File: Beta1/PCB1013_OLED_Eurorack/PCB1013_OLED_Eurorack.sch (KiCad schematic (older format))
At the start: 41 parts, among them J1 Axoloti_40Pin, J2 FPC_20POS, U1 MCP3008T-I/SL, U10 OLED_128x32_I2C, U2 MCP3008T-I/SL, U20 OLED_128x32_I2C, U3 I2C_1x4MUX_TCA9546A, U30 OLED_128x32_I2C, U40 OLED_128x32_I2C

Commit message: Rough placement
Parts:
- removed C1, C2: 0.1u, Capacitors_SMD:C_0603, symbol C
- removed CS_0_7, GND0, SPI_CLK_0, SPI_MISO_0, SPI_MOSI_0, VCC0: CONN_01X01, Liberry:single_0.1, symbol CONN_01X01
- removed JOY0, JOY1, JOY2, JOY3: XYJOY_Alps, Liberry:JOY_ALPS_RKJXV1224005, symbol XYJOY_Alps
- removed R0, R1, R2, R3, R4, R5, R6, R7: POT, Liberry:POT_ALPS_RK09K1130BM4, symbol POT
- removed U1, U2: MCP3008T-I/SL, Liberry:SOIC-16, symbol MCP3008T-I/SL
- added C4: 0.1u, Capacitor_SMD:C_0603_1608Metric, symbol Device:C
- added R4, RC1, RC50, RC60, RC70, RC80, RD1, RD50, RD60, RD70, RD80, RR1: 10K, Resistor_SMD:R_0603_1608Metric, symbol Device:R
- added U4: I2C_1x4MUX_TCA9546A, Liberry:SOIC-16_1.27x5.4, symbol PCB1013_OLED_Eurorack-rescue:I2C_1x4MUX_TCA9546A
- added U50, U60, U70, U80: OLED_128x32_I2C, Liberry:OLED_128x32, symbol PCB1013_OLED_Eurorack-rescue:OLED_128x32_I2C
- added U5000: STM32F103C8T6_BLUE_PILL, Liberry:BLUEPILL_CORTEXM3_STM32F103C8T6_THIN, symbol PCB1013_OLED_Eurorack:STM32F103C8T6_BLUE_PILL
- C3: symbol C -> Device:C
- J1: symbol Axoloti_40Pin -> PCB1013_OLED_Eurorack-rescue:Axoloti_40Pin
- J2: symbol FPC_20POS -> PCB1013_OLED_Eurorack-rescue:FPC_20POS
- RC0, RC10, RC20, RC30, RC40, RD0, RD10, RD20, RD30, RD40, RR0: footprint Resistors_SMD:R_0603 -> Resistor_SMD:R_0603_1608Metric; symbol R -> Device:R
- U10, U20, U30, U40: symbol OLED_128x32_I2C -> PCB1013_OLED_Eurorack-rescue:OLED_128x32_I2C
- U3: symbol I2C_1x4MUX_TCA9546A -> PCB1013_OLED_Eurorack-rescue:I2C_1x4MUX_TCA9546A
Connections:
- net labels added: I2C_SCL4, I2C_SCL5, I2C_SCL6, I2C_SCL7, I2C_SCL_AXO, I2C_SCL_EXT, I2C_SC_AXO, I2C_SDA4, I2C_SDA5, I2C_SDA6, I2C_SDA7, I2C_SDA_AXO, I2C_SDA_EXT, RESET_AXO, RX_AXO, RX_EXT, TX_AXO, TX_EXT
- net labels removed: I2C_SCL, I2C_SDA, JOY_0_0, JOY_0_1, JOY_1_0, JOY_1_1, JOY_2_0, JOY_2_1, JOY_3_0, JOY_3_1, P0, P1, P2, P3, P4, P5, P6, P7
- wire segments 234 -> 278

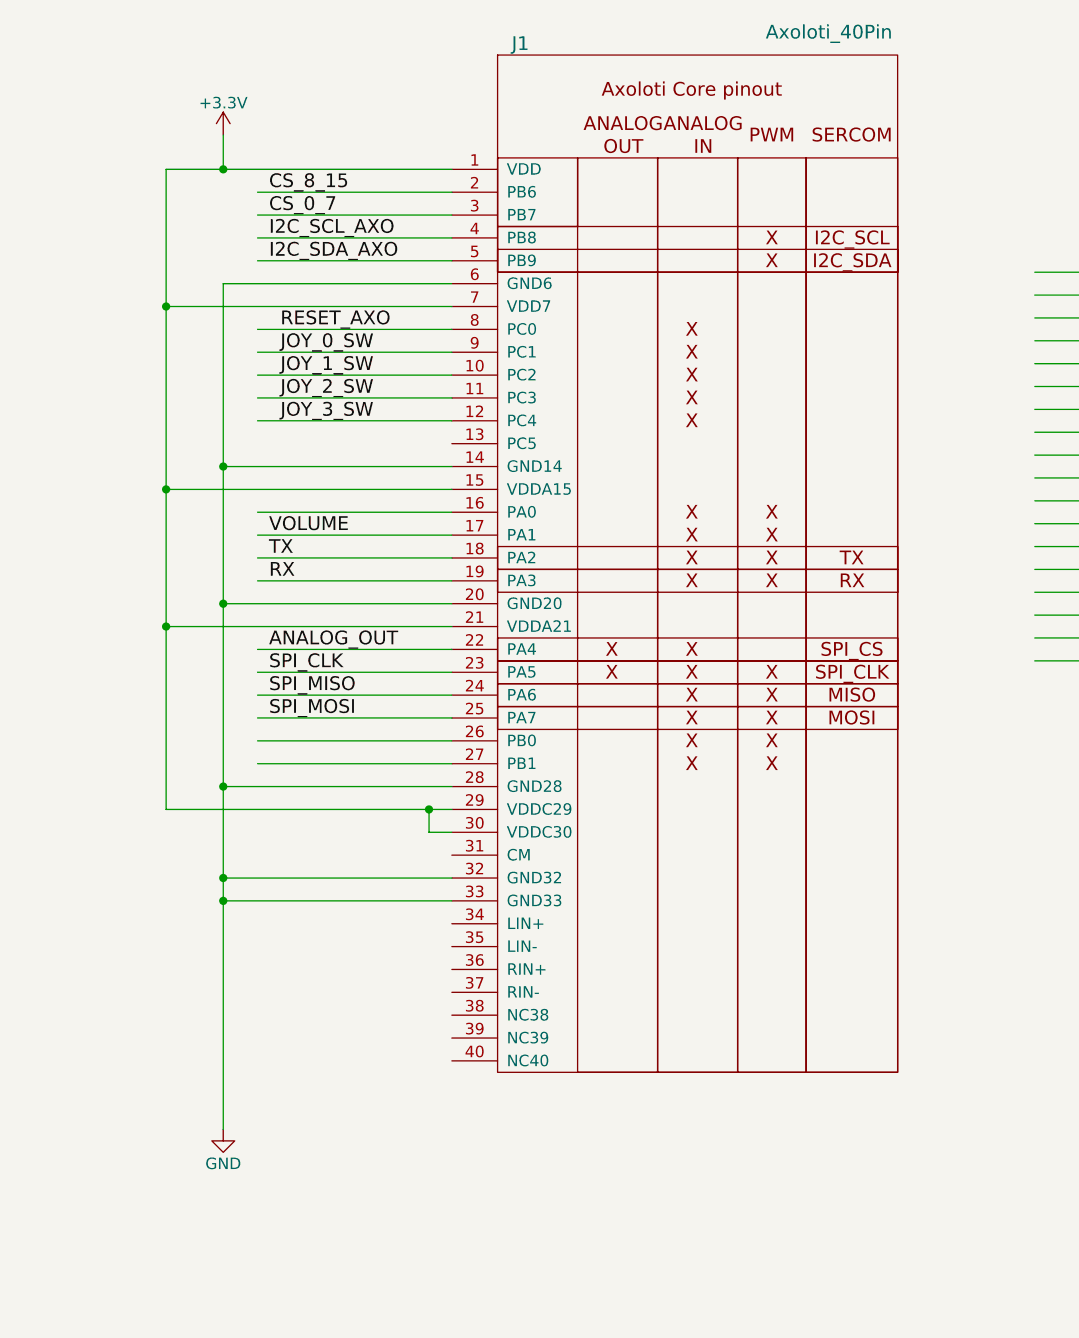
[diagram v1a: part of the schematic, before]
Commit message: Removed 40 pin header
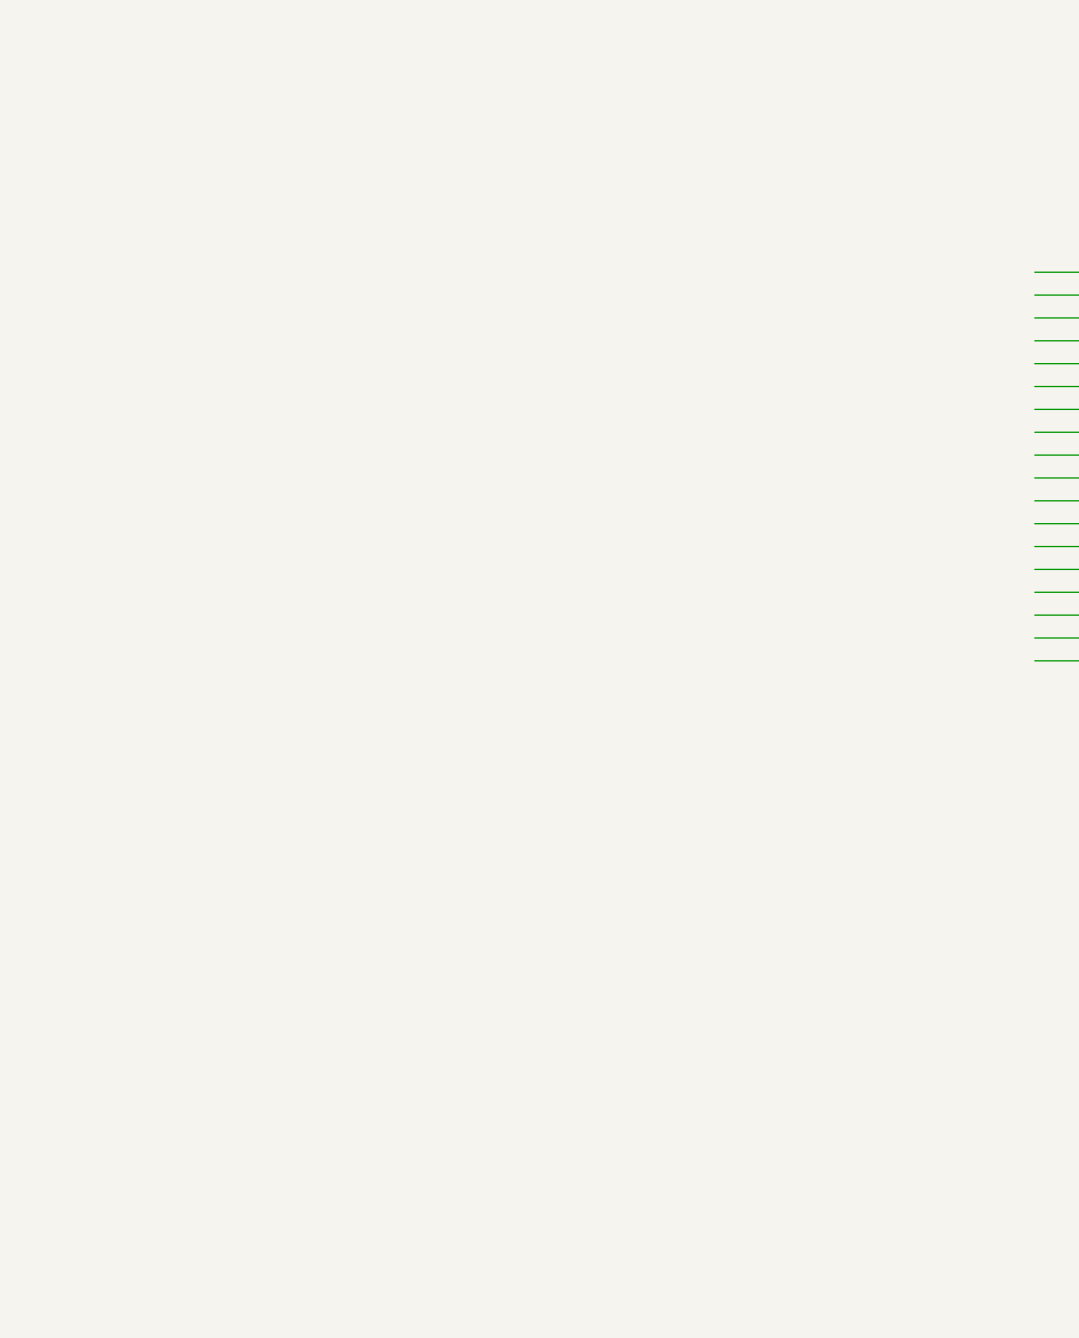
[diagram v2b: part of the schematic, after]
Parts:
- removed J1: Axoloti_40Pin, Liberry:Axoloti-40x1_slim, symbol PCB1013_OLED_Eurorack-rescue:Axoloti_40Pin
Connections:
- net labels removed: RX, TX
- wire segments 278 -> 233
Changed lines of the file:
@@
 Text Notes 30450 21350 0    60   ~ 0
 Date
-$Comp
-L PCB1013_OLED_Eurorack-rescue:Axoloti_40Pin J1
-U 1 1 591BA4F8
-P 22000 6350
-F 0 "J1" H 22300 11850 60  0000 C CNN
-F 1 "Axoloti_40Pin" H 23650 11900 60  0000 C CNN
-F 2 "Liberry:Axoloti-40x1_slim" H 18550 9300 60  0001 C CNN
-F 3 "" H 18550 9300 60  0001 C CNN
-	1    22000 6350
-	1    0    0    -1
-$EndComp
-Text Label 21200 1700 0    60   ~ 0
-I2C_SCL_AXO
-Text Label 21200 1800 0    60   ~ 0
-I2C_SDA_AXO
-$Comp
-L power:GND #PWR06
-U 1 1 591BA513
-P 21000 5600
-F 0 "#PWR06" H 21000 5350 50  0001 C CNN
-F 1 "GND" H 21000 5450 50  0000 C CNN
-F 2 "" H 21000 5600 50  0000 C CNN
-F 3 "" H 21000 5600 50  0000 C CNN
-	1    21000 5600
-	1    0    0    -1
-$EndComp
-Text Label 21200 3800 0    60   ~ 0
-SPI_MOSI
-Text Label 21200 3700 0    60   ~ 0
-SPI_MISO
-Text Label 21200 3600 0    60   ~ 0
-SPI_CLK
-Text Label 21250 2200 0    60   ~ 0
-JOY_0_SW
-Text Label 21250 2300 0    60   ~ 0
-JOY_1_SW
-Text Label 21200 1600 0    60   ~ 0
-CS_0_7
-Text Label 21200 1500 0    60   ~ 0
-CS_8_15
-$Comp
-L power:+3.3V #PWR07
-U 1 1 591E099F
-P 21000 1250
-F 0 "#PWR07" H 21000 1100 50  0001 C CNN
-F 1 "+3.3V" H 21000 1390 50  0000 C CNN
-F 2 "" H 21000 1250 50  0000 C CNN
-F 3 "" H 21000 1250 50  0000 C CNN
-	1    21000 1250
-	1    0    0    -1
-$EndComp
-Wire Wire Line
-	21150 1800 22000 1800
-Wire Wire Line
-	21150 1700 22000 1700
-Wire Wire Line
-	20750 1400 21000 1400
-Wire Wire Line
-	21000 1900 21000 2700
-Wire Wire Line
-	21000 4600 22000 4600
-Wire Wire Line
-	21000 4500 22000 4500
-Connection ~ 21000 4600
-Wire Wire Line
-	21000 4100 22000 4100
-Connection ~ 21000 4500
-Wire Wire Line
-	21000 3300 22000 3300
-Connection ~ 21000 4100
-Wire Wire Line
-	21000 2700 22000 2700
-Connection ~ 21000 3300
-Wire Wire Line
-	21000 1900 22000 1900
-Connection ~ 21000 2700
-Wire Wire Line
-	20750 2000 22000 2000
-Wire Wire Line
-	20750 3400 22000 3400
-Wire Wire Line
-	20750 4200 21900 4200
-Wire Wire Line
-	22000 4300 21900 4300
-Wire Wire Line
-	21900 4300 21900 4200
-Connection ~ 21900 4200
-Wire Wire Line
-	21150 3600 22000 3600
-Wire Wire Line
-	21150 3700 22000 3700
-Wire Wire Line
-	21150 3800 22000 3800
-Wire Wire Line
-	21150 2100 22000 2100
-Wire Wire Line
-	21150 2200 22000 2200
-Wire Wire Line
-	21150 3900 22000 3900
-Wire Wire Line
-	21150 1600 22000 1600
-Wire Wire Line
-	21150 1500 22000 1500
-Wire Wire Line
-	21000 1400 21000 1250
-Wire Wire Line
-	20750 1400 20750 2000
-Connection ~ 21000 1400
-Connection ~ 20750 2000
-Connection ~ 20750 2800
-Connection ~ 20750 3400
-Wire Wire Line
-	22000 4000 21150 4000
-Text Label 21200 3000 0    60   ~ 0
-VOLUME
-Wire Wire Line
-	21150 3000 22000 3000
-Wire Wire Line
-	22000 2400 21150 2400
-Wire Wire Line
-	22000 2500 21150 2500
-Wire Wire Line
-	22000 2900 21150 2900
 Text Label 25650 3150 0    60   ~ 0
 SPI_MOSI
@@
 Wire Wire Line
 	24550 1850 26100 1850
-Wire Wire Line
-	22000 3500 21150 3500
-Text Label 21200 3500 0    60   ~ 0
-ANALOG_OUT
-Text Label 21250 2100 0    60   ~ 0
-RESET_AXO
-Text Label 21250 2400 0    60   ~ 0
-JOY_2_SW
-Text Label 21250 2500 0    60   ~ 0
-JOY_3_SW
 Text Notes 24750 2050 0    60   ~ 0
 PC0
@@
 Text Notes 24750 2450 0    60   ~ 0
 PC4
-Wire Wire Line
-	22000 2300 21150 2300
-Wire Wire Line
-	22000 2800 20750 2800
-Wire Wire Line
-	22000 3100 21150 3100
-Wire Wire Line
-	22000 3200 21150 3200
-Text Label 21200 3100 0    60   ~ 0
-TX
-Text Label 21200 3200 0    60   ~ 0
-RX
 $Comp
 L Device:R RD10
@@
 Connection ~ 28050 10350
 Wire Wire Line
-	21000 4600 21000 5600
-Wire Wire Line
-	21000 4500 21000 4600
-Wire Wire Line
-	21000 4100 21000 4500
-Wire Wire Line
-	21000 3300 21000 4100
-Wire Wire Line
-	21000 2700 21000 3300
-Wire Wire Line
-	21900 4200 22000 4200
-Wire Wire Line
-	21000 1400 22000 1400
-Wire Wire Line
-	20750 2000 20750 2800
-Wire Wire Line
-	20750 2800 20750 3400
-Wire Wire Line
-	20750 3400 20750 4200
-Wire Wire Line
 	26100 1750 26100 1850
